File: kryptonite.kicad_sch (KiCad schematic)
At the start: 27 parts, among them J1 Conn_01x04_Pin, P2 USB_C_Plug, SW1 SW_SPDT, SW2 SW_Push, U1 STM32F072CBUx, U2 ATECC608A-MAHDA, U3 MCP1700x-330xxTT, Y1 8MHz

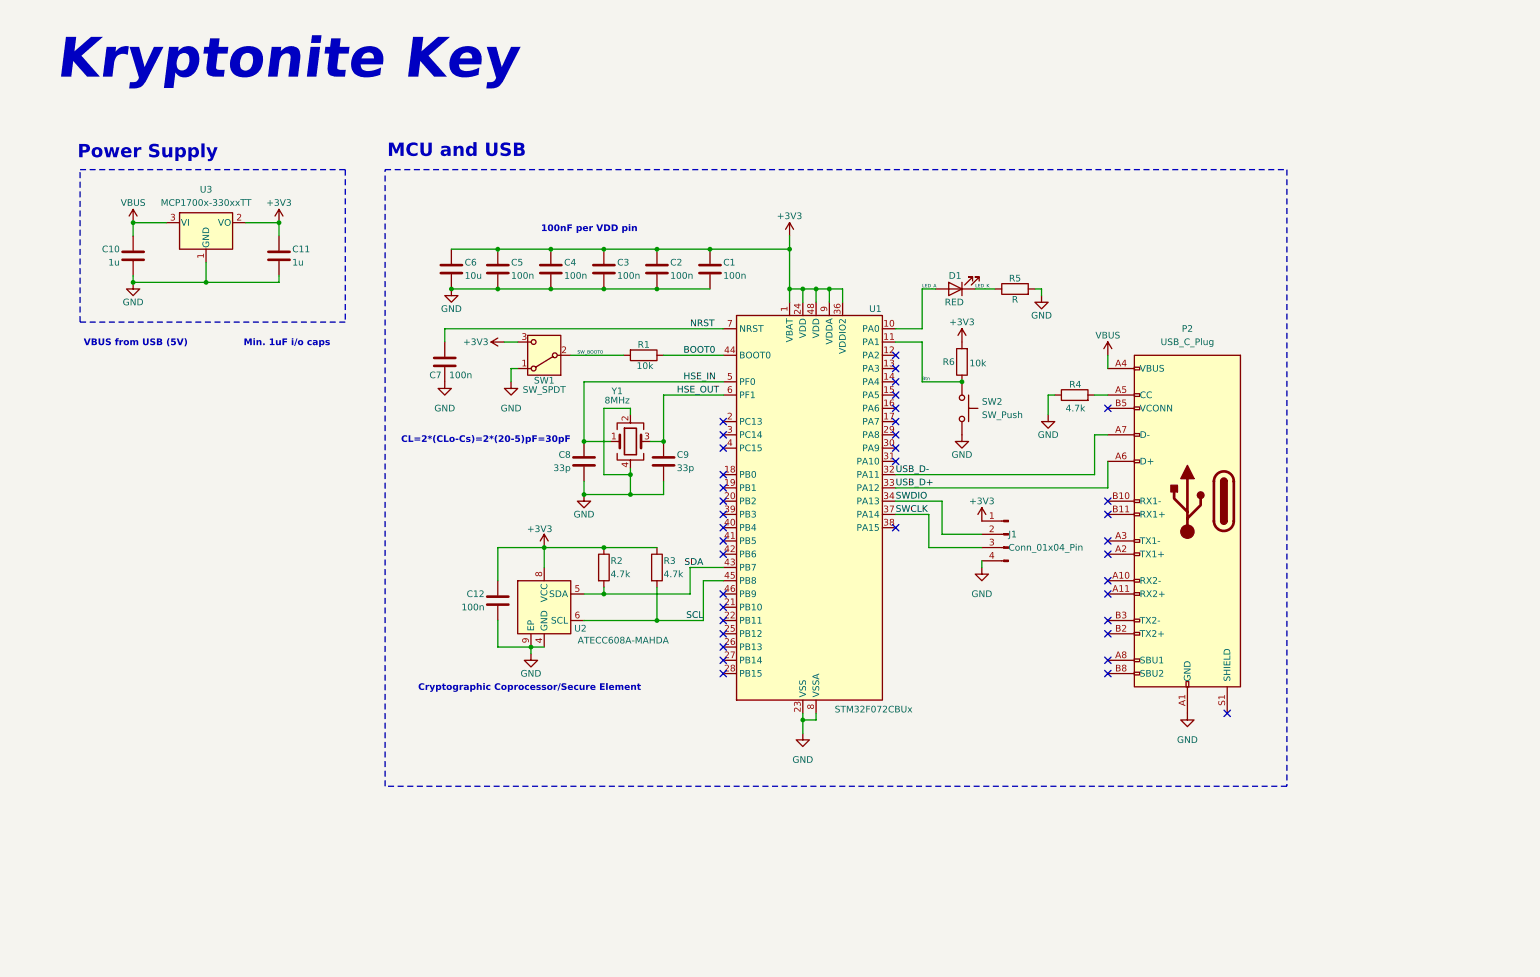
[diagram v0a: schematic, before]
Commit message: Added ESD protection
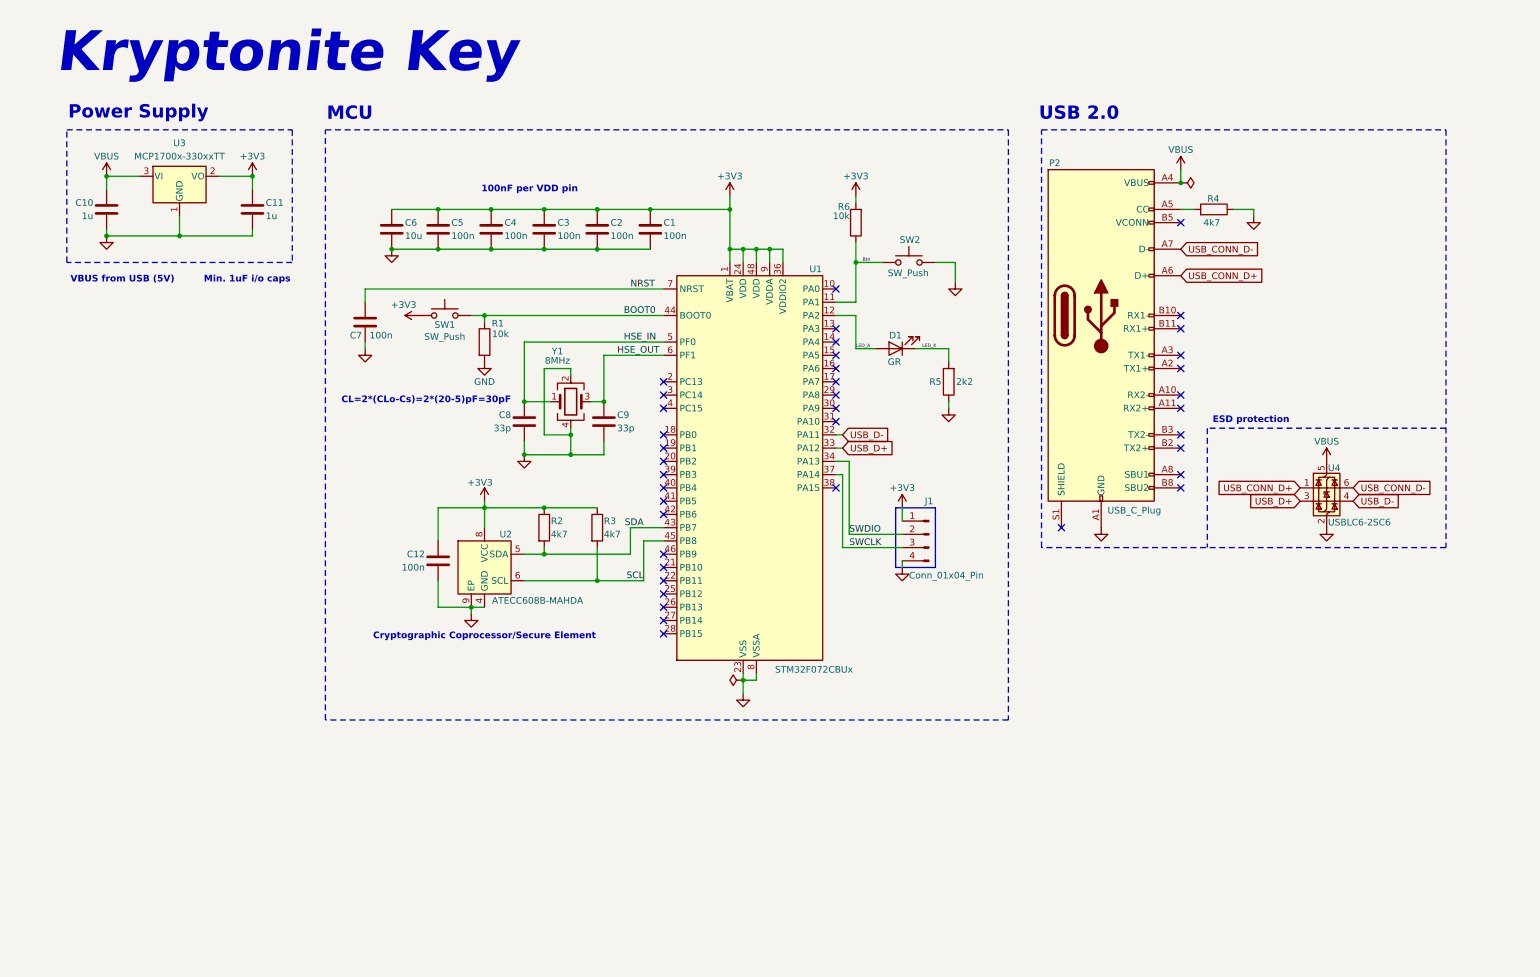
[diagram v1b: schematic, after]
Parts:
- removed SW1: SW_SPDT, symbol Switch:SW_SPDT
- added SW1: SW_Push, Button_Switch_SMD:SW_Push_1P1T_XKB_TS-1187A, symbol Switch:SW_Push
- added U4: USBLC6-2SC6, Package_TO_SOT_SMD:SOT-23-6, symbol Power_Protection:USBLC6-2SC6
- C1, C12, C2, C3, C4, C5, C7, C8, C9: footprint (none) -> Capacitor_SMD:C_0402_1005Metric_Pad0.74x0.62mm_HandSolder
- C10, C11, C6: footprint (none) -> Capacitor_SMD:C_0805_2012Metric_Pad1.18x1.45mm_HandSolder
- D1: value RED -> GR; footprint (none) -> LED_SMD:LED_0603_1608Metric_Pad1.05x0.95mm_HandSolder
- J1: footprint (none) -> Connector_PinHeader_2.54mm:PinHeader_1x04_P2.54mm_Vertical
- R1, R6: footprint (none) -> Resistor_SMD:R_0402_1005Metric_Pad0.72x0.64mm_HandSolder
- R2, R3, R4: value 4.7k -> 4k7; footprint (none) -> Resistor_SMD:R_0402_1005Metric_Pad0.72x0.64mm_HandSolder
- R5: value R -> 2k2; footprint (none) -> Resistor_SMD:R_0402_1005Metric_Pad0.72x0.64mm_HandSolder
- SW2: footprint (none) -> Button_Switch_SMD:SW_Push_1P1T_XKB_TS-1187A
- U2: value ATECC608A-MAHDA -> ATECC608B-MAHDA; symbol Security:ATECC608A-MAHDA -> Security:ATECC608B-MAHDA
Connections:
- net SW_BOOT0 is gone; now on net GND: R1.2
- net +3V3: now also SW1.1
- net BOOT0: now also SW1.2
- net GND: now also R5.1, U4.2 (GND); no longer R5.2
- net LED_A: now also U1.12 (PA2); no longer U1.10 (PA0)
- net LED_K: now also R5.2; no longer R5.1
- net USB_D+: now also U4.3 (I/O2); no longer P2.A6 (D+)
- net USB_D-: now also U4.4 (I/O2); no longer P2.A7 (D-)
- net VBUS: now also U4.5 (VBUS)
- new net USB_CONN_D+: P2.A6 (D+), U4.1 (I/O1)
- new net USB_CONN_D-: P2.A7 (D-), U4.6 (I/O1)
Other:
- note added: "ESD protection"
- note added: "MCU"
- note added: "USB 2.0"
- note removed: "MCU and USB"
- moved on the sheet: C1, C10, C11, C12, C2, C3, C4, C5, C6, C7, C8, C9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

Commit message: did some stuff
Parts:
- removed P2: USB_C_Plug, symbol Connector:USB_C_Plug
- removed SW1: SW_Push, Button_Switch_SMD:SW_Push_1P1T_XKB_TS-1187A, symbol Switch:SW_Push
- added P1: USB_C_Plug_USB2.0, type-c:TYPE-C-31-G-01, symbol Connector:USB_C_Plug
- C1: renamed from C6; footprint Capacitor_SMD:C_0805_2012Metric_Pad1.18x1.45mm_HandSolder -> Capacitor_SMD:C_0603_1608Metric
- C10: renamed from C12; footprint Capacitor_SMD:C_0402_1005Metric_Pad0.74x0.62mm_HandSolder -> Capacitor_SMD:C_0402_1005Metric
- C11: renamed from C10; value 1u -> 10u; footprint Capacitor_SMD:C_0805_2012Metric_Pad1.18x1.45mm_HandSolder -> Capacitor_SMD:C_0603_1608Metric
- C12: renamed from C11; value 1u -> 10u; footprint Capacitor_SMD:C_0805_2012Metric_Pad1.18x1.45mm_HandSolder -> Capacitor_SMD:C_0603_1608Metric
- C2: renamed from C5; footprint Capacitor_SMD:C_0402_1005Metric_Pad0.74x0.62mm_HandSolder -> Capacitor_SMD:C_0402_1005Metric
- C3: renamed from C4; footprint Capacitor_SMD:C_0402_1005Metric_Pad0.74x0.62mm_HandSolder -> Capacitor_SMD:C_0402_1005Metric
- C4: renamed from C3; footprint Capacitor_SMD:C_0402_1005Metric_Pad0.74x0.62mm_HandSolder -> Capacitor_SMD:C_0402_1005Metric
- C5: renamed from C2; footprint Capacitor_SMD:C_0402_1005Metric_Pad0.74x0.62mm_HandSolder -> Capacitor_SMD:C_0402_1005Metric
- C6: renamed from C1; footprint Capacitor_SMD:C_0402_1005Metric_Pad0.74x0.62mm_HandSolder -> Capacitor_SMD:C_0402_1005Metric
- C7, C8, C9: footprint Capacitor_SMD:C_0402_1005Metric_Pad0.74x0.62mm_HandSolder -> Capacitor_SMD:C_0402_1005Metric
- D1: Distributer Link (none) -> https://www.lcsc.com/product-detail/Light-Emitting-Diodes-L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; Manufacturer (none) -> XINGLIGHT; Manufacturer Part Number (none) -> XL-1608SURC-06
- J1: Distributer Link (none) -> https://www.lcsc.com/product-detail/Pin-Headers_CONNFLY-Ele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; Manufacturer (none) -> CONNFLY; Manufacturer Part Number (none) -> DS1021-1x4SF11-B
- R1: footprint Resistor_SMD:R_0402_1005Metric_Pad0.72x0.64mm_HandSolder -> Resistor_SMD:R_0402_1005Metric; Distributer Link (none) -> https://www.lcsc.com/product-detail/Chip-Resistor-Surface-M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; Manufacturer (none) -> YAGEO; Manufacturer Part Number (none) -> RC0402FR-0710KL
- R2, R3, R4: footprint Resistor_SMD:R_0402_1005Metric_Pad0.72x0.64mm_HandSolder -> Resistor_SMD:R_0402_1005Metric; Distributer Link (none) -> https://www.lcsc.com/product-detail/Chip-Resistor-Surface-M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; Manufacturer (none) -> UNI-ROYAL(Uniroyal Elec); Manufacturer Part Number (none) -> 0402WGJ0472TCE
- R5: renamed from R6; footprint Resistor_SMD:R_0402_1005Metric_Pad0.72x0.64mm_HandSolder -> Resistor_SMD:R_0402_1005Metric; Distributer Link (none) -> https://www.lcsc.com/product-detail/Chip-Resistor-Surface-M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; Manufacturer (none) -> YAGEO; Manufacturer Part Number (none) -> RC0402FR-0710KL
- R6: renamed from R5; value 2k2 -> 68; footprint Resistor_SMD:R_0402_1005Metric_Pad0.72x0.64mm_HandSolder -> Resistor_SMD:R_0402_1005Metric; Distributer Link (none) -> https://www.lcsc.com/product-detail/Chip-Resistor-Surface-M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; Manufacturer (none) -> FOJAN; Manufacturer Part Number (none) -> FRC0402J680 TS
- SW1: renamed from SW2; Distributer Link (none) -> https://www.lcsc.com/product-detail/Tactile-Switches_XKB-Co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; Manufacturer (none) -> XKB Connection; Manufacturer Part Number (none) -> TS-1187A-B-A-B
- U1: Distributer Link (none) -> https://www.lcsc.com/product-detail/Microcontrollers-MCU-MP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; Manufacturer (none) -> STMicroelectronics; Manufacturer Part Number (none) -> STM32F072CBU6
- U2: Distributer Link (none) -> https://www.lcsc.com/product-detail/Security-Verification-E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; Manufacturer (none) -> Microchip Tech; Manufacturer Part Number (none) -> ATECC608B-MAHDA-S
- U3: Distributer Link (none) -> https://www.lcsc.com/product-detail/Voltage-Regulators-Line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; Manufacturer (none) -> Microchip Tech; Manufacturer Part Number (none) -> MCP1700T-3302E/TT
- U4: Distributer Link (none) -> https://www.lcsc.com/product-detail/ESD-and-Surge-Protectio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; Manufacturer (none) -> STMicroelectronics; Manufacturer Part Number (none) -> USBLC6-2SC6
- Y1: Distributer Link (none) -> https://www.lcsc.com/product-detail/Crystals_Yajingxin-TAXM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; Manufacturer (none) -> Yajingxin; Manufacturer Part Number (none) -> TAXM8M4RLBDDT2T
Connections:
- net BOOT0: now also R1.2; no longer R1.1
- net GND: now also R1.1, P1.A1 (GND), P1.A12 (GND), P1.B1 (GND), P1.B12 (GND), P1.S1 (SHIELD); no longer R1.2
- net LED_A: now also U1.15 (PA5); no longer U1.12 (PA2)
- net SCL: now also U1.21 (PB10); no longer U1.45 (PB8)
- net SDA: now also U1.22 (PB11); no longer U1.43 (PB7)
- net USB_CONN_D+: now also U4.3 (I/O2), P1.A6 (D+); no longer U4.1 (I/O1)
- net USB_CONN_D-: now also U4.1 (I/O1), P1.A7 (D-); no longer U4.6 (I/O1)
- net USB_D+: now also U4.4 (I/O2); no longer U4.3 (I/O2)
- net USB_D-: now also U4.6 (I/O1); no longer U4.4 (I/O2)
- net VBUS: now also P1.A4 (VBUS), P1.A9 (VBUS), P1.B4 (VBUS), P1.B9 (VBUS)
- net at R4.2: now also P1.A5 (CC)
- net BTN: now reaches U1.16 (PA6)
- net BTN: now also R5.1, SW1.1
- removed net Btn: R5.1, SW1.1, U1.11 (PA1)
- no-connect marks 39 -> 38
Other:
- note added: "+5V to +3V3 LDO Regulator"
- note added: "100nF per VDD pin, 10uF bulk capacitor"
- note added: "Cryptographic Coprocessor/Secure Element (I^{2}C)"
- note added: "I_{F} = 20mA V_{F} = 2.3V V_{S} = 3.3V R = (V_{S} - V_{F}) / I_{F} = (3.3V - 2.3V) / 20mA = 50"
- note added: "Kryptonite"
- note added: "LED indicator"
- note added: "Min. 1uF i/o ceramic capacitors"
- note added: "Notes"
- note added: "SWD pins"
- note added: "USB Connector and ESD Protection"
- note added: "User presence button"
- note removed: "100nF per VDD pin"
- note removed: "Cryptographic Coprocessor/Secure Element"
- note removed: "Kryptonite Key"
- note removed: "MCU"
- note removed: "Min. 1uF i/o caps"
- note removed: "USB 2.0"
- title: Kryptonite Key -> Kryptonite
- moved on the sheet: C1, C10, C11, C12, C2, C3, C4, C5, C6, C7, C8, C9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

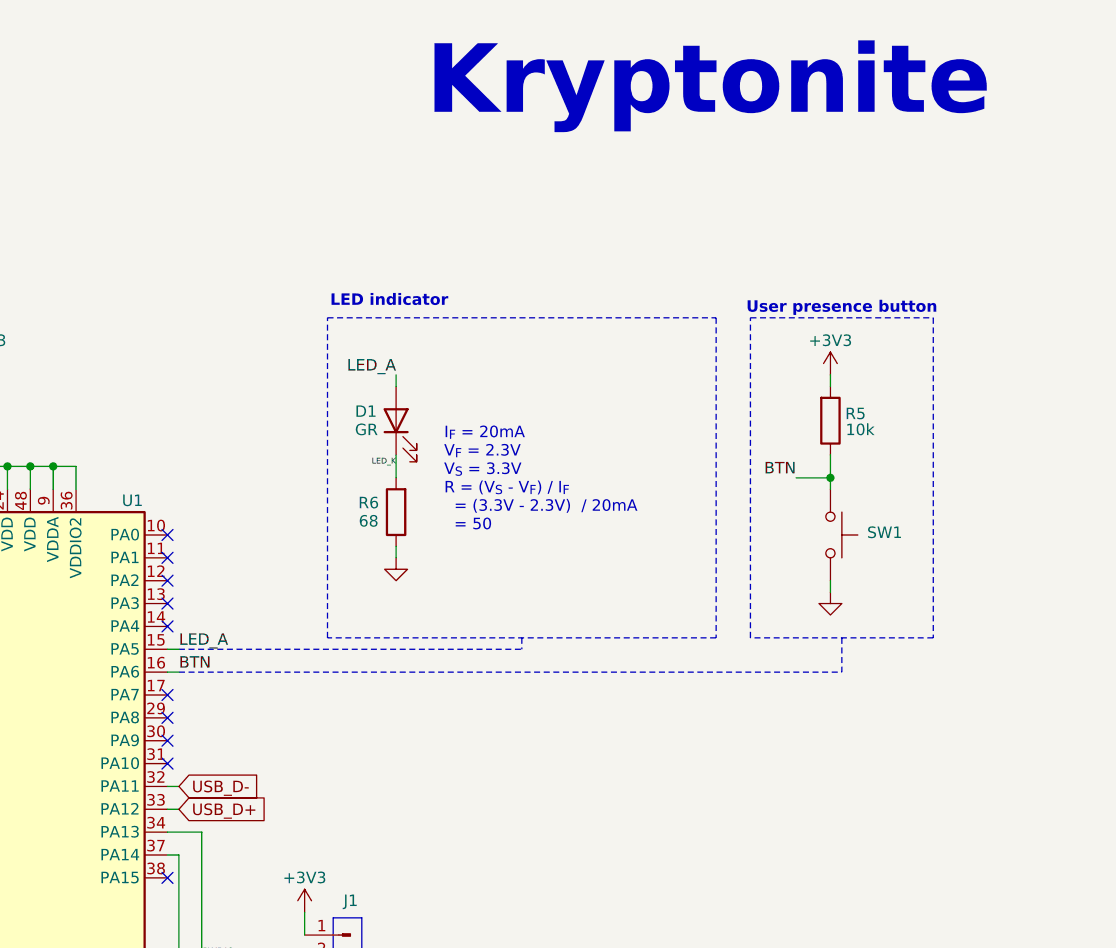
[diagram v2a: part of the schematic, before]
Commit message: Finalized PCB layout and added gerbers
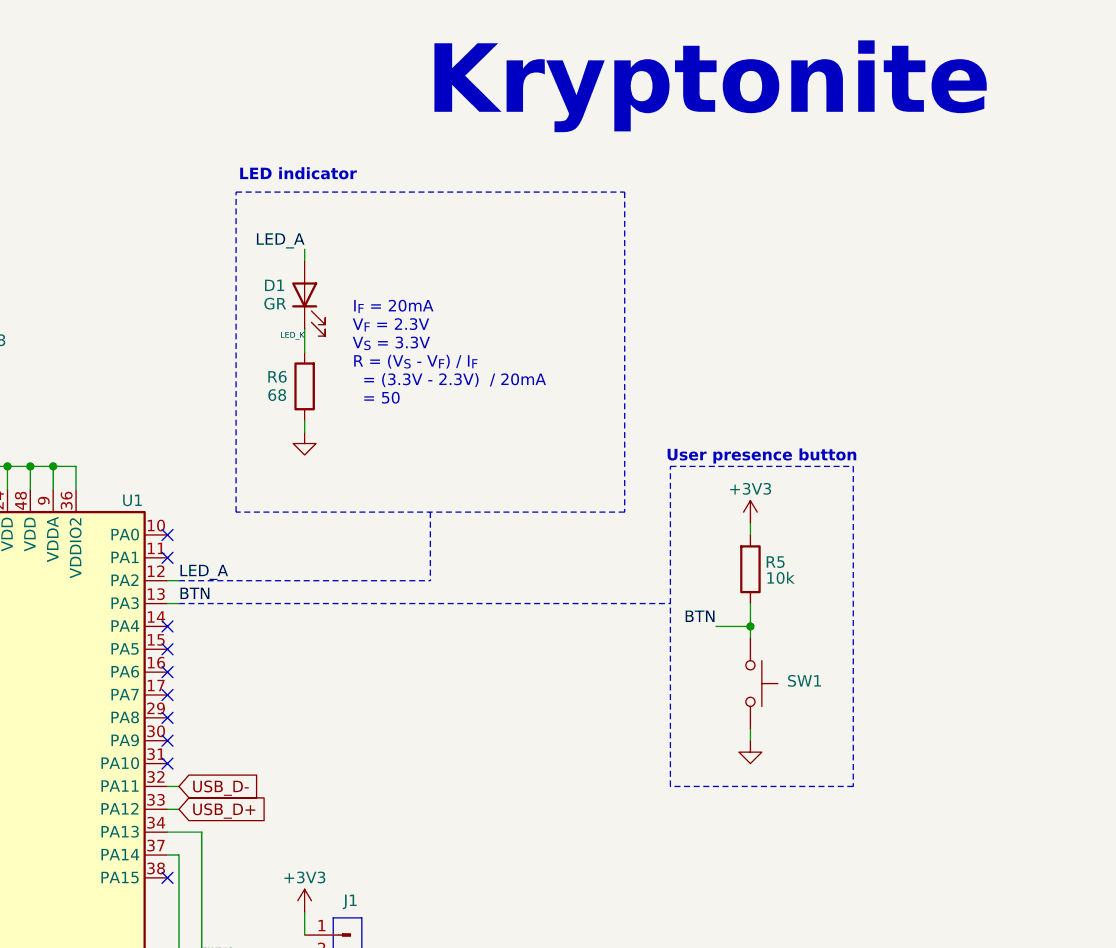
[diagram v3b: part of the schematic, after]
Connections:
- net BTN: now also U1.13 (PA3); no longer U1.16 (PA6)
- net LED_A: now also U1.12 (PA2); no longer U1.15 (PA5)
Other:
- moved on the sheet: D1, R5, R6, SW1

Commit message: Add files via upload
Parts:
- C1, C11, C12: Distributer Link (none) -> https://www.lcsc.com/product-detail/Multilayer-Ceramic-Capa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; LCSC (none) -> C466781; Manufacturer (none) -> SANYEAR; Manufacturer Part Number (none) -> C0603X5R106M160NT
- C10, C2, C3, C4, C5, C6, C7: Distributer Link (none) -> https://www.lcsc.com/product-detail/Multilayer-Ceramic-Capa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; LCSC (none) -> C6119799; Manufacturer (none) -> HRE; Manufacturer Part Number (none) -> CGA0402X7R104K160GT
- C8, C9: Distributer Link (none) -> https://www.lcsc.com/product-detail/Multilayer-Ceramic-Capa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; LCSC (none) -> C696910; Manufacturer (none) -> CCTC; Manufacturer Part Number (none) -> TCC0402COG330J500AT
- D1: LCSC (none) -> C965799
- J1: LCSC (none) -> C7430360
- P1: LCSC (none) -> C530605; Manufacturer Korean Hroparts Elec -> Korean Hroparts Elec
- R1, R5: LCSC (none) -> C60490
- R2, R3, R4: LCSC (none) -> C25940
- R6: LCSC (none) -> C2906961
- SW1: LCSC (none) -> C318884
- U1: LCSC (none) -> C92504
- U2: LCSC (none) -> C1518773
- U3: LCSC (none) -> C39051
- U4: LCSC (none) -> C7519
- Y1: LCSC (none) -> C720915
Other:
- note removed: "ESD protection"
- moved on the sheet: U4
